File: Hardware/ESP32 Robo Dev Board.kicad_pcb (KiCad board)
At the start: 2 copper layers, 61.3 x 61.3 mm, 61 parts, among them J1 PRG, U1 ESP32-S3-WROOM-1, U2 AMS1117-3.3, U3 STSPIN250, U4 STSPIN250

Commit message: More robots (and cleanups)
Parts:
- S1, S2, S3, S4, S5, S6, S7, S8: value TCRT5000L -> TCRT1010_VIS
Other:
- board text added: "${FULL_REVISION}"

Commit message: Fixup! Better anotations
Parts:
- S1, S2, S3, S4, S5, S6, S7, S8: value TCRT1010_VIS -> TCRT5000L

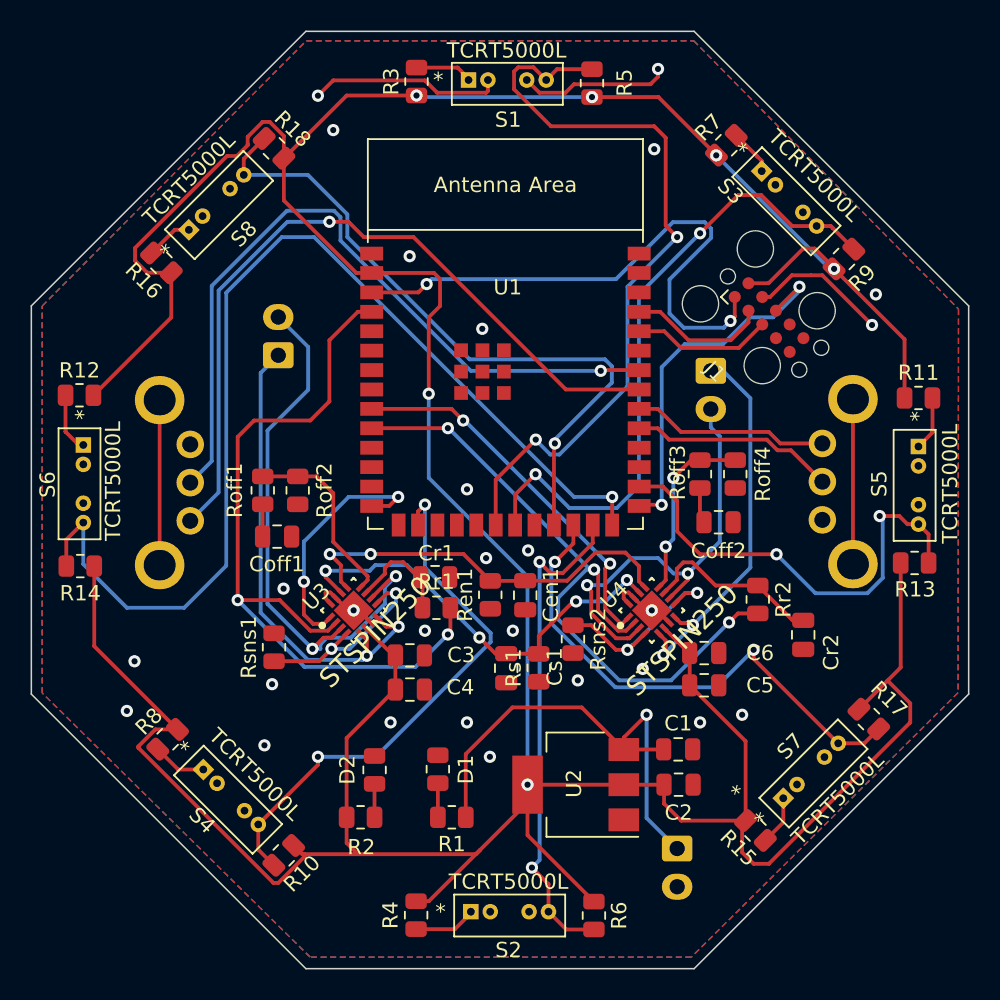
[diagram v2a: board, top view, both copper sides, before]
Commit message: Fix Range Finder Locations
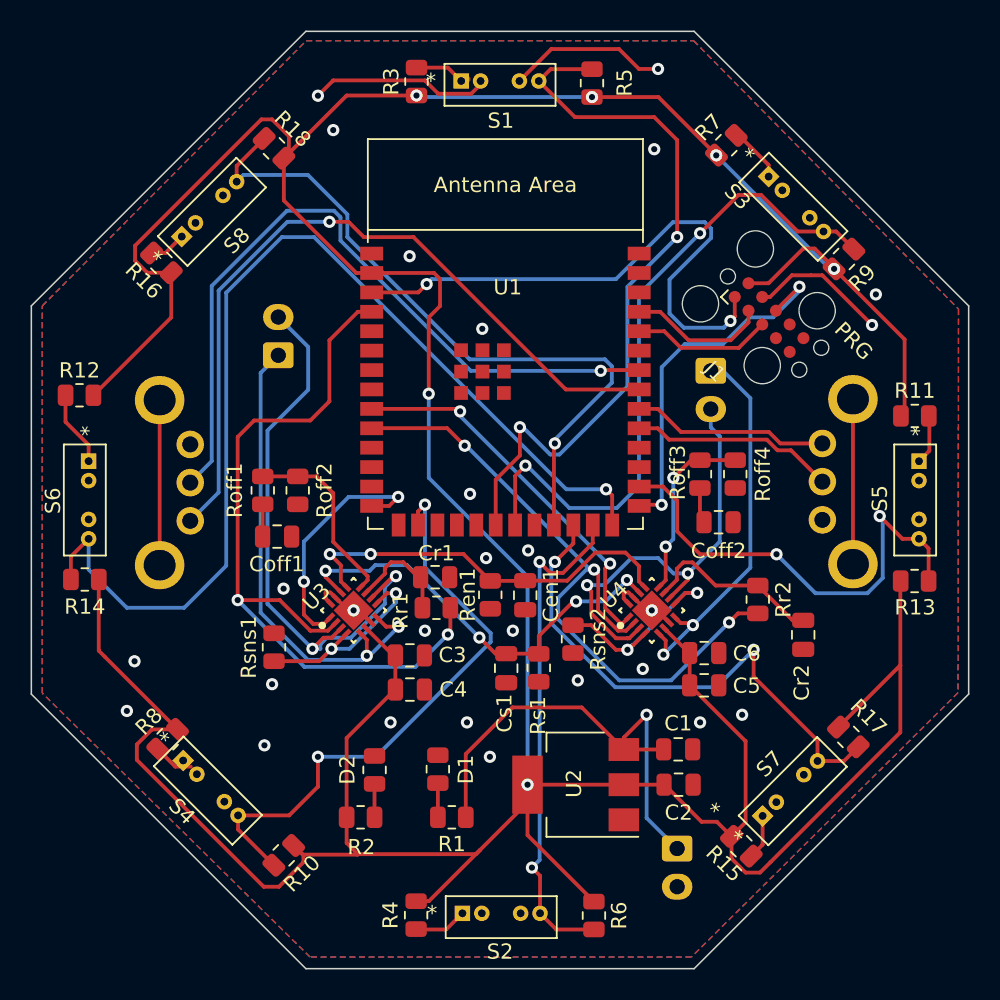
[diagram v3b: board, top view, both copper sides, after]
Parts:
- added REF**: OSHW-Logo2_7.3x6mm_SilkScreen, Symbol:OSHW-Logo2_7.3x6mm_SilkScreen, B.Cu at (127.5, 85.7)
- moved G*** 10.2 mm to (138.9, 83.8), turned to 180 degrees
- moved S2 1.91 mm to (138.7, 114.8)
- moved S7 1.78 mm to (155.8, 108.4)
- moved R17 1.78 mm to (161.4, 103.2)
- moved S4 1.45 mm to (117.9, 104.7)
- moved R15 1.38 mm to (154.4, 110.3)
- moved R11 1.20 mm to (165.8, 82.2)
- moved R13 1.18 mm to (165.8, 93.0)
- moved S6 1.12 mm to (111.7, 85.2)
- moved S5 0.96 mm to (166.1, 85.2)
- moved R14 0.93 mm to (111.5, 92.9)
- moved S8 0.64 mm to (117.8, 70.5)
- moved S3 0.58 mm to (156.2, 66.5)
- moved S1 0.48 mm to (136.1, 60.3)
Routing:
- net +3V3: track 284.3 -> 287.3 mm
- net /IR6: track 35.8 -> 38.9 mm
- net /IR1: track 51.1 -> 48.6 mm
- net /IR7: track 71.2 -> 69.9 mm
- net /IR8: track 45.0 -> 46.3 mm
- net /IR2: track 42.9 -> 44.1 mm
- net Net-(R12-Pad2): track 3.91 -> 4.94 mm
- net Net-(R8-Pad2): track 3.54 -> 2.64 mm
- net Net-(R7-Pad2): track 3.03 -> 3.68 mm
- net Net-(R16-Pad2): track 3.07 -> 2.42 mm
- net /IR3: track 30.1 -> 30.8 mm
- net Net-(R4-Pad2): track 4.11 -> 3.48 mm
- net /IR4: track 34.5 -> 35.1 mm
- net Net-(R15-Pad2): track 3.24 -> 2.73 mm
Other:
- board text added: "Design By Arthur W. Aznive Jr. https://github.com/Amoskeag/RoboDojo {dblquote}Even the smallest things are worth building!{dblquote}"
- board text added: "JLCJLCJLCJLC"

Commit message: Rebuild Layout
Took the V1.0 Layout and reworked it.
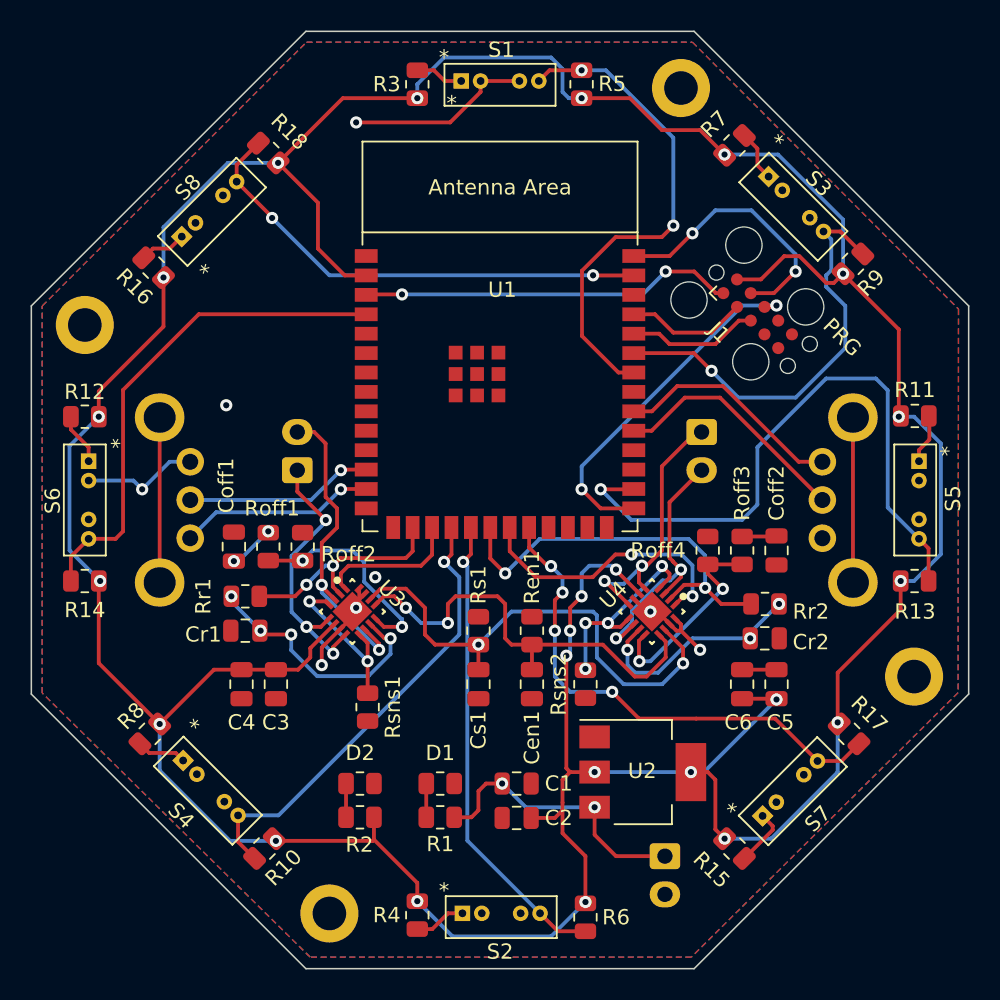
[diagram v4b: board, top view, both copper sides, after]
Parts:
- added ?: , , F.Cu at (111.5, 76.2)
- added ?: , , F.Cu at (150.5, 60.8)
- added ?: , , F.Cu at (165.8, 99.2)
- added ?: , , F.Cu at (127.5, 114.8)
- moved REF** 13.7 mm to (139.0, 93.0)
- moved Cr1 12.9 mm to (122.0, 96.2), turned to 180 degrees
- moved Rr1 12.5 mm to (122.0, 94.0)
- moved C4 11.0 mm to (121.8, 99.8), turned to -90 degrees
- moved C2 10.8 mm to (139.8, 108.5), turned to 180 degrees
- moved C1 10.8 mm to (139.8, 106.2)
- moved C3 8.97 mm to (124.0, 99.8), turned to 90 degrees
- moved J_A1 7.62 mm to (125.4, 85.8)
- moved Rsns1 7.27 mm to (130.0, 101.2), turned to -90 degrees
- moved Cen1 5.84 mm to (140.8, 99.8)
- moved Roff3 5.71 mm to (154.5, 91.0), turned to 90 degrees
- moved Roff4 5.31 mm to (152.2, 91.0), turned to 90 degrees
- moved C5 4.73 mm to (156.8, 99.8), turned to -90 degrees
- moved Rs1 4.64 mm to (137.2, 96.2), turned to -90 degrees
- moved U2 4.47 mm to (148.0, 105.5), turned to 0 degrees
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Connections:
- E1 pad 2: /L_Signal_A -> /R_Signal_A
- E1 pad 3: /L_Signal_B -> /R_Signal_B
- E2 pad 2: /R_Signal_A -> /L_Signal_A
- E2 pad 3: /R_Signal_B -> /L_Signal_B
- U1 pad 10: /PWM B -> unconnected-(U1-Pad10)
- U1 pad 12: unconnected-(U1-Pad12) -> /L_Signal_A
- U1 pad 13: unconnected-(U1-Pad13) -> /L_Signal_B
- U1 pad 14: /PHA -> unconnected-(U1-Pad14)
- U1 pad 16: /IR6 -> /PWM A
- U1 pad 17: unconnected-(U1-Pad17) -> /PHA
- U1 pad 18: unconnected-(U1-Pad18) -> /IR6
- U1 pad 19: unconnected-(U1-Pad19) -> /IR5
- U1 pad 20: /IR1 -> /PWM B
- U1 pad 21: /IR2 -> /PHB
- U1 pad 22: unconnected-(U1-Pad22) -> /IR4
- U1 pad 23: /IR8 -> unconnected-(U1-Pad23)
- U1 pad 24: /IR4 -> unconnected-(U1-Pad24)
- U1 pad 25: /IR5 -> unconnected-(U1-Pad25)
- U1 pad 26: /IR7 -> unconnected-(U1-Pad26)
- U1 pad 31: /L_Signal_A -> /R_Signal_A
- U1 pad 32: /L_Signal_B -> /R_Signal_B
- U1 pad 33: /R_Signal_B -> unconnected-(U1-Pad33)
- U1 pad 34: /R_Signal_A -> /IR1
- U1 pad 35: unconnected-(U1-Pad35) -> /IR2
- U1 pad 39: unconnected-(U1-Pad39) -> /IR8
- U1 pad 4: /PWM A -> /IR7
- U1 pad 9: /PHB -> unconnected-(U1-Pad9)
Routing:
- net /IR7: track 69.9 -> 32.9 mm, vias 1 -> 0
- net /PWM A: track 50.9 -> 14.9 mm
- net /R_Signal_B: track 49.8 -> 15.1 mm, vias 1 -> 0
- net /R_Signal_A: track 48.7 -> 16.0 mm, vias 1 -> 0
- net /PWM B: track 45.4 -> 26.2 mm, vias 3 -> 2
- net /Motor Controller Left/Motor_Out1: track 37.7 -> 21.0 mm
- net +3V3: track 287.3 -> 270.7 mm, vias 6 -> 23
- net /IR1: track 48.6 -> 32.5 mm
- net /IR2: track 44.1 -> 28.1 mm, vias 2 -> 1
- net /IR8: track 46.3 -> 31.7 mm, vias 1 -> 2
- net /Motor Controller Left/Motor_Out2: track 31.9 -> 18.1 mm, vias 2 -> 3
- net Net-(C1-Pad1): track 32.0 -> 18.5 mm, vias 1 -> 2
- net GND: track 40.2 -> 52.9 mm, vias 27 -> 10
- net /Enable: track 37.2 -> 24.6 mm
- net /IR3: track 30.8 -> 41.7 mm, vias 2 -> 1
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
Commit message: Update ESP32 Robo Dev Board.kicad_pcb
Update Silkscreen, Move Components to better fit silkscreen
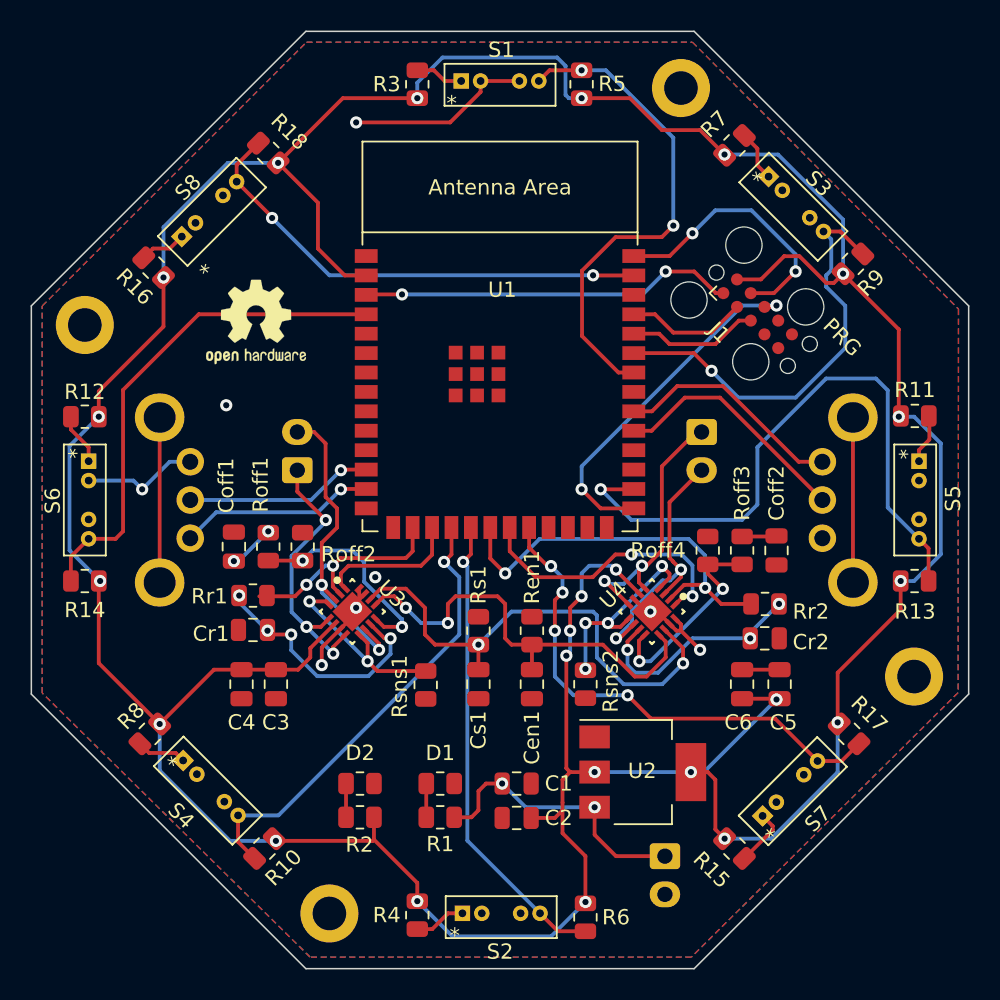
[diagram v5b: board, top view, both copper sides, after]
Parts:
- REF**: moved to F.Cu
- moved REF** 23.5 mm to (122.7, 76.0), turned to 0 degrees
- moved Rsns1 4.07 mm to (133.8, 99.8)
- moved Cr1 0.50 mm to (122.5, 96.2)
- moved Rr1 0.50 mm to (122.5, 94.0)
- moved C5 0.20 mm to (156.9, 99.8)
- gave numbers to parts that had none: 4
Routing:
- net Net-(Rsns1-Pad1): track 10.9 -> 12.9 mm

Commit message: Add I2C IC
Added TCA9548A mux interface
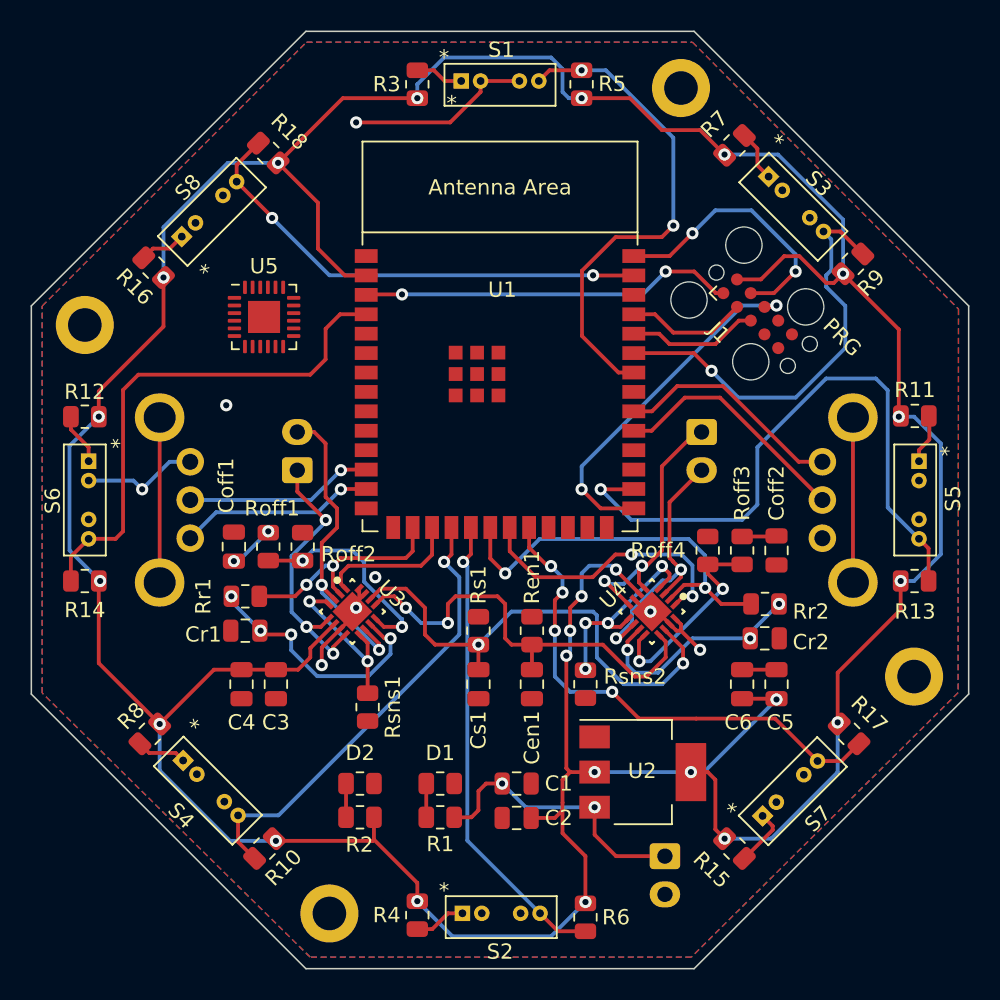
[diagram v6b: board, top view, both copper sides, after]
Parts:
- added U5: TCA9548ARGER, Package_DFN_QFN:Texas_RGE0024C_EP2.1x2.1mm, F.Cu at (123.2, 75.7)
- REF**: moved to B.Cu
- moved REF** 17.1 mm to (138.2, 69.0), turned to 180 degrees
- moved Rsns1 4.07 mm to (130.0, 101.2)
- moved Cr1 0.50 mm to (122.0, 96.2)
- moved Rr1 0.50 mm to (122.0, 94.0)
- moved C5 0.20 mm to (156.8, 99.8)
- renumbered M1 to ?, M2 to ?, M4 to ?, M3 to ?
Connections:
- U1 pad 20: /PWM B -> /SCL
- U1 pad 21: /PHB -> /SDA
- U1 pad 24: unconnected-(U1-Pad24) -> /PHB
- U1 pad 25: unconnected-(U1-Pad25) -> /PWM B
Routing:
- net Net-(Rsns1-Pad1): track 12.9 -> 10.9 mm
- net /IR7: track 32.9 -> 34.1 mm
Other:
- board text added: "Design By Arthur W. Aznive Jr. https://github.com/Amoskeag/RoboDojo"
- board text added: "{dblquote}Even the smallest things are worth building!{dblquote}"
- board text removed: "Design By Arthur W. Aznive Jr. https://github.com/Amoskeag/RoboDojo {dblquote}Even the smallest things are worth building!{dblquote}"

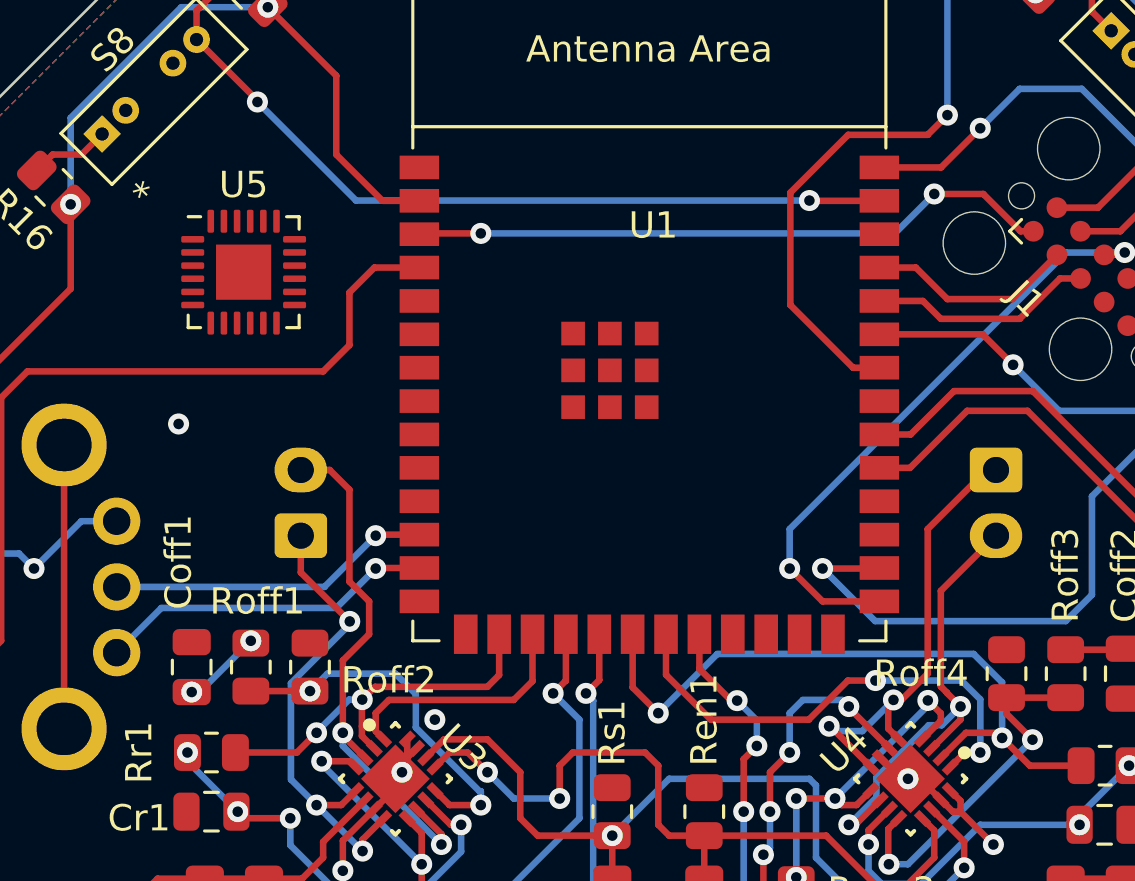
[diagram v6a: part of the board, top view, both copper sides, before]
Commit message: Update ESP32 Robo Dev Board.kicad_pcb
Add in TCA9548A Multiplexer.

Reroute traces.

Prepare for Proximity Sensor overhaul
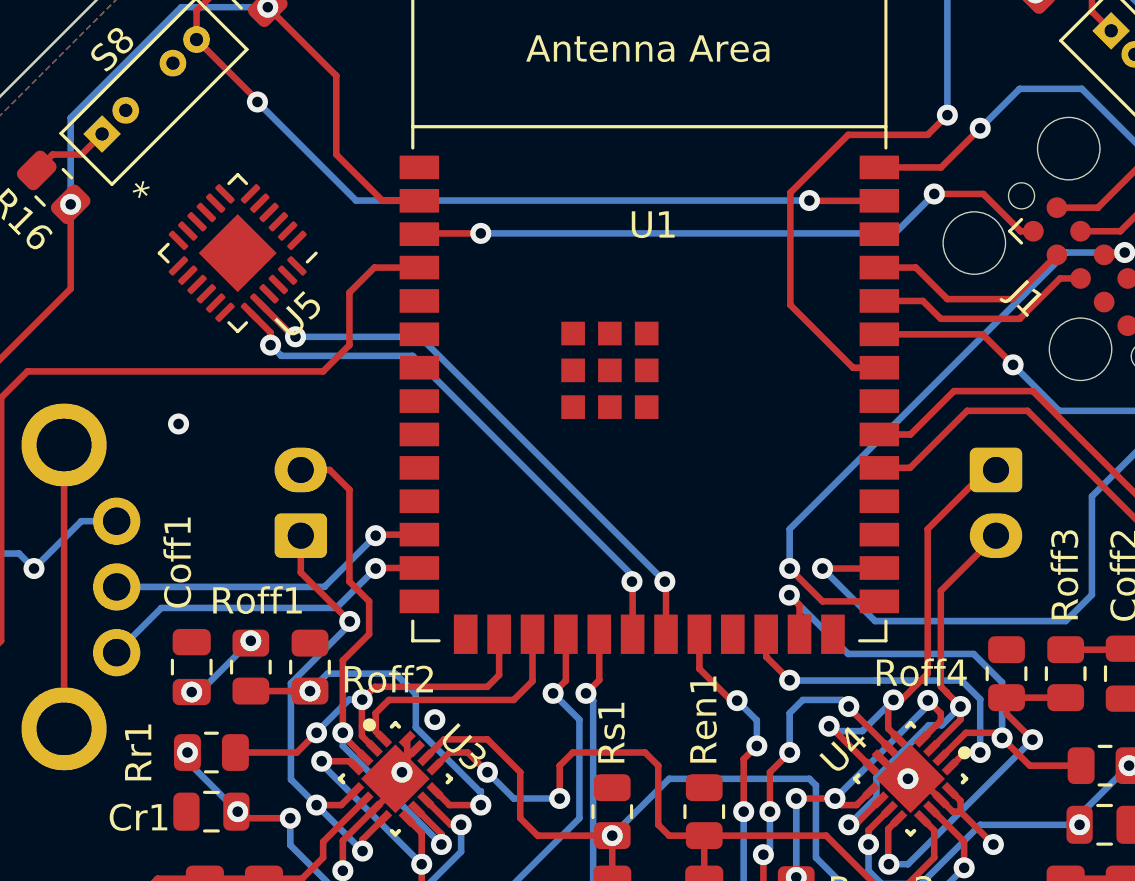
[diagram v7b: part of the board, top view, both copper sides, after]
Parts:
- moved U5 0.76 mm to (123.0, 75.0), turned to -135 degrees
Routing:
- net /SDA: track 0.00 -> 21.8 mm, vias 0 -> 2
- net /SCL: track 0.00 -> 21.2 mm, vias 0 -> 2
- net /PWM B: track 26.2 -> 19.5 mm
- net /PHB: track 18.5 -> 13.1 mm
